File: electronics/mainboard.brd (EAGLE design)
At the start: 158.8 x 159.4 mm, 88 parts, among them T1 NPN_BC817,215, T2 NPN_BC817,215, T3 NPN_BC817,215, U1 CD4051BM, X1 JST-XH-10-PIN-LONG-PAD, X2 JST-XH-10-PIN-LONG-PAD, X3 JST-XH-10-PIN-LONG-PAD, X4 JST-XH-10-PIN-LONG-PAD, X5 JST-XH-10-PIN-LONG-PAD

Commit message: Board tweaks
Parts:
- added CA1, CA2, CA3, CA4, CA5, CA6, CA7: C_EU-100NF, rhoban:C0805
- moved R22 8.35 mm to (22.9, -36.2)
- moved R23 8.35 mm to (20.3, -36.2)
- moved C5 6.02 mm to (37.7, -33.9)
- moved C6 6.02 mm to (41.3, -33.9)
- moved XTAL4 6.02 mm to (39.4, -29.8)
- moved C3 5.85 mm to (8.26, -34.3)
- moved C4 5.85 mm to (12.1, -34.3)
- moved XTAL3 5.85 mm to (10.2, -29.8)
- moved ENC4 4.84 mm to (40.0, -21.0)
- moved ENC3 3.81 mm to (10.2, -20.3)
- moved U$4 2.54 mm to (17.8, -56.5)
- moved C1 2.01 mm to (-21.0, -34.3)
- moved C2 2.01 mm to (-16.5, -34.3)
- moved ENC2 2.01 mm to (-19.1, -20.3)
- moved XTAL2 2.01 mm to (-19.1, -29.8)
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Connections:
- net 3.3: now also CA1.1, CA3.1
- net GND: now also CA1.2, CA2.2, CA3.2, CA4.2, CA5.2, CA6.2, CA7.2
- net VCC: now also CA2.1, CA4.1, CA5.1, CA6.1, CA7.1
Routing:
- net GND: track 18.7 -> 26.1 mm

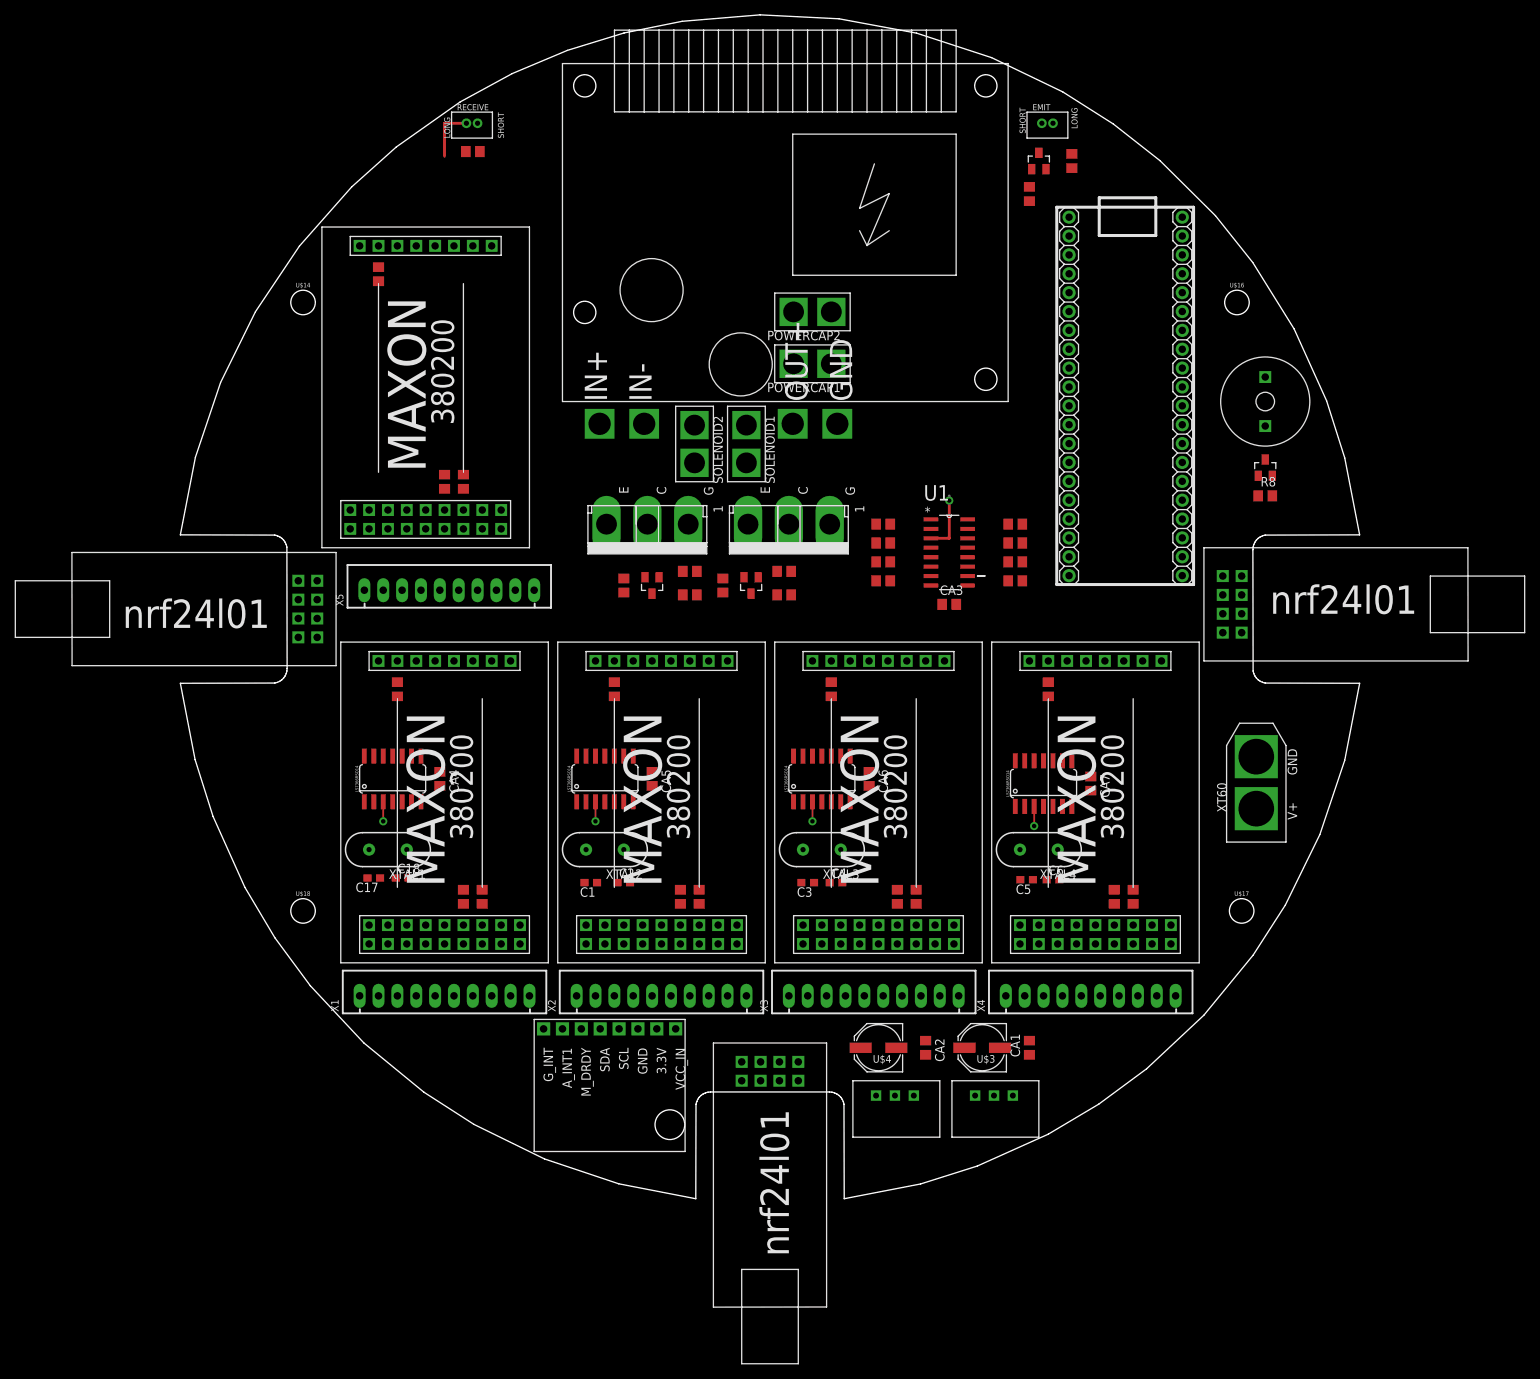
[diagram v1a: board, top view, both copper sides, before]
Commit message: 2nd xt60 connector
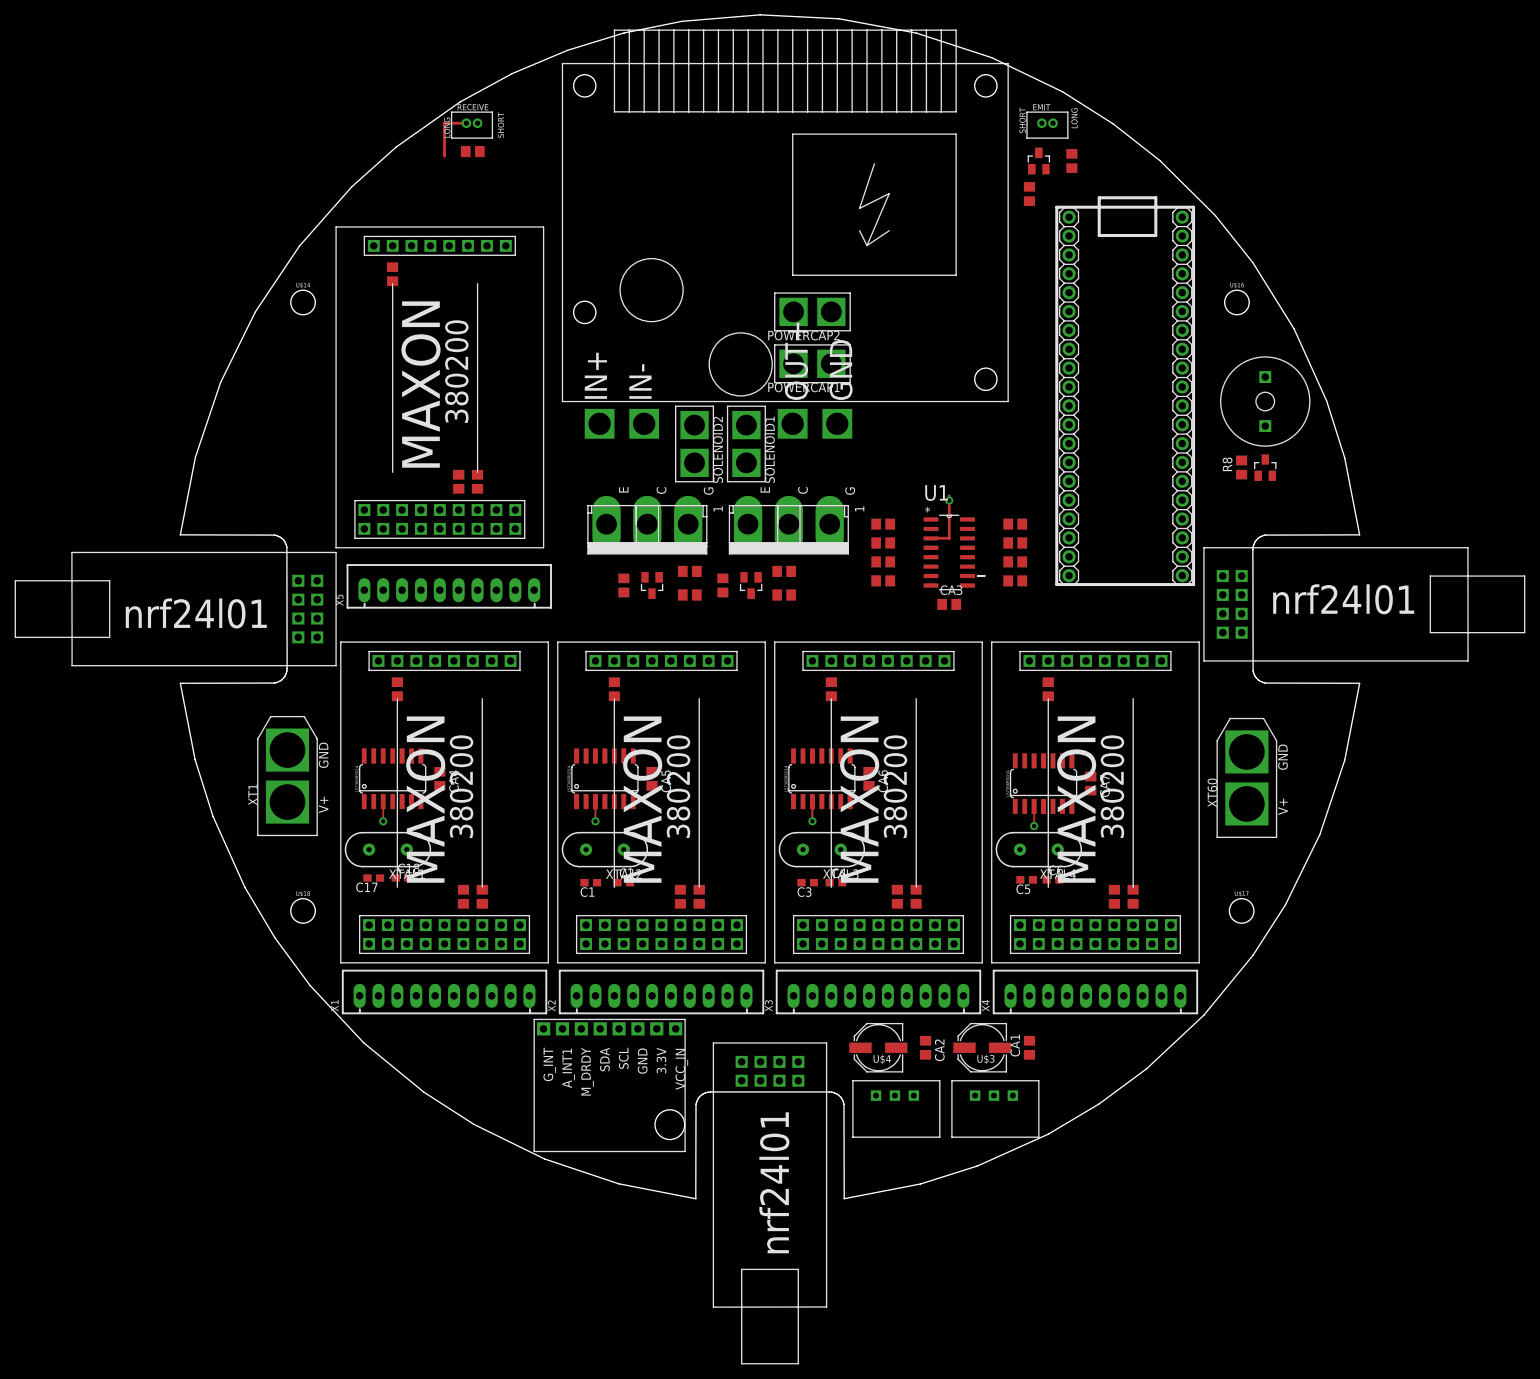
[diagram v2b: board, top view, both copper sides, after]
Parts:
- added XT1: CONNEC_ALIM, rhoban:XT60
- moved R8 4.96 mm to (66.7, 21.6), turned to 90 degrees
- moved U$10 1.91 mm to (-31.1, 13.3)
- moved R28 1.91 mm to (-36.2, 19.7)
- moved R29 1.91 mm to (-38.7, 19.7)
- moved R30 1.91 mm to (-47.6, 47.6)
- moved XT60 1.42 mm to (71.4, -28.2)
- moved X4 0.64 mm to (47.0, -49.5)
- moved X3 0.64 mm to (17.8, -49.5)
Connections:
- net GND: now also XT1.GND
- net VIN: now also XT1.V+

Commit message: README
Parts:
- R5: value 60 -> 62
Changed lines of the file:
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@@
 <element name="T2" library="rhoban" package="SOT-23" value="NPN_BC817,215" x="39.37" y="62.865"/>
 <element name="R4" library="rhoban" package="R0805" value="1K" x="38.1" y="58.42" rot="R90"/>
-<element name="R5" library="rhoban" package="R0805" value="60" x="43.815" y="62.865" rot="R90"/>
+<element name="R5" library="rhoban" package="R0805" value="62" x="43.815" y="62.865" rot="R90"/>
 <element name="R6" library="rhoban" package="R0805" value="10K" x="-36.83" y="64.135"/>
 <element name="ENC1" library="rhoban" package="SO14" value="LS7366RSO14" x="-47.625" y="-20.32"/>

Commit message: Re aligning holes
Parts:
- moved U$17 0.44 mm to (66.2, -38.1)
- moved U$16 0.20 mm to (66.2, 43.8)
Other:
- board text added: "RHOBAN SSL rev0"
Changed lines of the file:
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@@
 <setting verticaltext="up"/>
 </settings>
-<grid distance="0.635" unitdist="mm" unit="mm" style="lines" multiple="1" display="no" altdistance="0.025" altunitdist="inch" altunit="inch"/>
+<grid distance="0.1" unitdist="mm" unit="mm" style="lines" multiple="1" display="no" altdistance="0.025" altunitdist="inch" altunit="inch"/>
 <layers>
 <layer number="1" name="Top" color="4" fill="1" visible="yes" active="yes"/>
@@
 <rectangle x1="-62.865" y1="40.64" x2="-56.515" y2="46.99" layer="41"/>
 <rectangle x1="-62.865" y1="40.64" x2="-56.515" y2="46.99" layer="42"/>
-<rectangle x1="62.865" y1="40.64" x2="69.215" y2="46.99" layer="41"/>
-<rectangle x1="62.865" y1="40.64" x2="69.215" y2="46.99" layer="42"/>
-<rectangle x1="63.5" y1="-41.275" x2="69.85" y2="-34.925" layer="41"/>
-<rectangle x1="63.5" y1="-41.275" x2="69.85" y2="-34.925" layer="42"/>
+<rectangle x1="63.065" y1="40.64" x2="69.415" y2="46.99" layer="41"/>
+<rectangle x1="63.065" y1="40.64" x2="69.415" y2="46.99" layer="42"/>
+<rectangle x1="63.2" y1="-41.275" x2="69.55" y2="-34.925" layer="41"/>
+<rectangle x1="63.2" y1="-41.275" x2="69.55" y2="-34.925" layer="42"/>
 <rectangle x1="-62.865" y1="-41.275" x2="-56.515" y2="-34.925" layer="41"/>
 <rectangle x1="-62.865" y1="-41.275" x2="-56.515" y2="-34.925" layer="42"/>
+<text x="-59.055" y="15.24" size="1.778" layer="21" rot="R90">RHOBAN SSL rev0</text>
 </plain>
 <attributes>
@@
 <element name="SOLENOID2" library="rhoban" package="CONNEC_1X02_BIG" value="CONNEC_1X02BIG" x="-6.985" y="27.305" rot="R270"/>
 <element name="U$14" library="SparkFun-Hardware" package="STAND-OFF" value="" x="-59.69" y="43.815"/>
-<element name="U$16" library="SparkFun-Hardware" package="STAND-OFF" value="" x="66.04" y="43.815"/>
-<element name="U$17" library="SparkFun-Hardware" package="STAND-OFF" value="" x="66.675" y="-38.1"/>
+<element name="U$16" library="SparkFun-Hardware" package="STAND-OFF" value="" x="66.24" y="43.815"/>
+<element name="U$17" library="SparkFun-Hardware" package="STAND-OFF" value="" x="66.24" y="-38.1"/>
 <element name="U$18" library="SparkFun-Hardware" package="STAND-OFF" value="" x="-59.69" y="-38.1"/>
 <element name="CA2" library="rhoban" package="C0805" value="C_EU-100NF" x="24.13" y="-56.515" rot="R270">

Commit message: Updating board
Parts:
- R5: value 62 -> 110
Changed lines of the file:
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@@
 <element name="T2" library="rhoban" package="SOT-23" value="NPN_BC817,215" x="39.37" y="62.865"/>
 <element name="R4" library="rhoban" package="R0805" value="1K" x="38.1" y="58.42" rot="R90"/>
-<element name="R5" library="rhoban" package="R0805" value="62" x="43.815" y="62.865" rot="R90"/>
+<element name="R5" library="rhoban" package="R0805" value="110" x="43.815" y="62.865" rot="R90"/>
 <element name="R6" library="rhoban" package="R0805" value="10K" x="-36.83" y="64.135"/>
 <element name="ENC1" library="rhoban" package="SO14" value="LS7366RSO14" x="-47.625" y="-20.32"/>
